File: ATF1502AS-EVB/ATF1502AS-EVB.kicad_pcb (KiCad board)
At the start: 2 copper layers, 25.4 x 50.8 mm, 17 parts, among them J1 Conn_02x03_Odd_Even, J2 Conn_01x20, J3 Conn_01x20, U1 ATF1502AS

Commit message: Update for upstream changes.
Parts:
- U1: value ATF1502AS -> ATF1502AS-xAx44

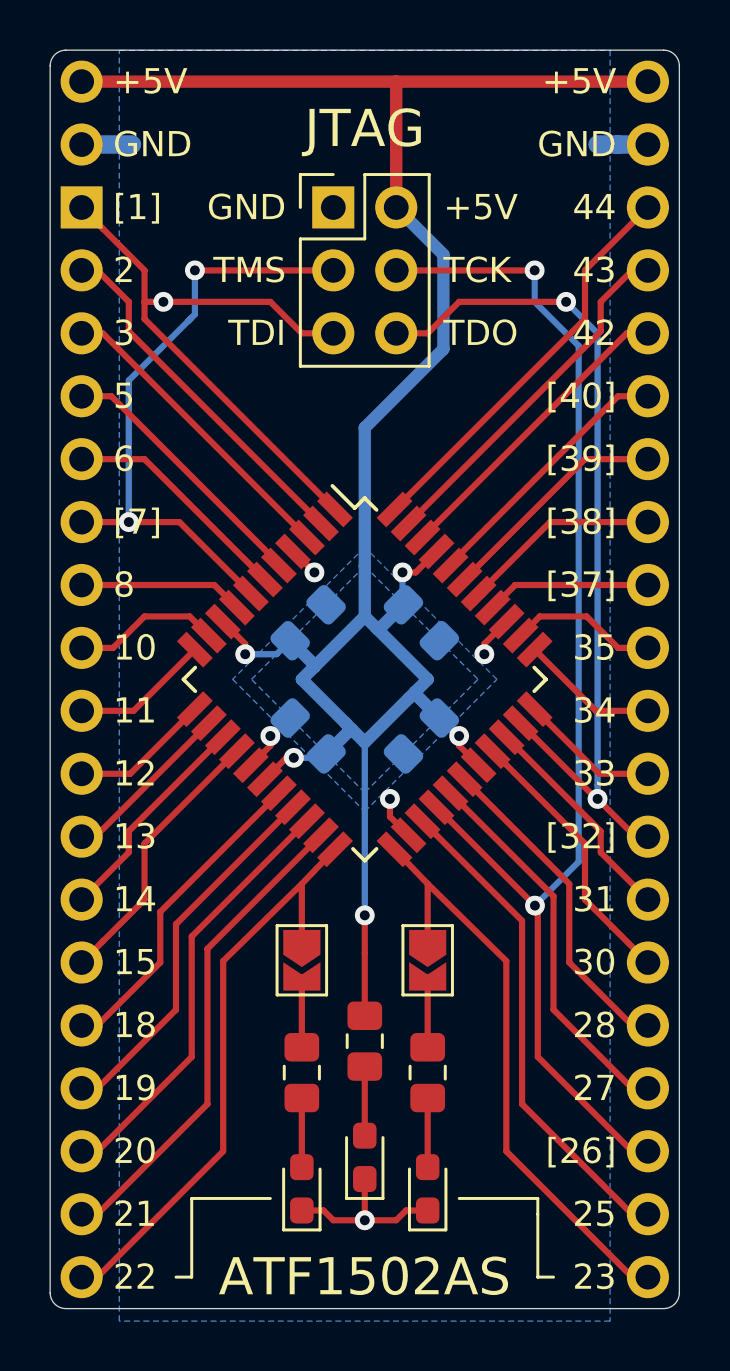
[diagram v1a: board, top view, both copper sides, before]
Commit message: ATF1502AS-EVB: final changes for fab.
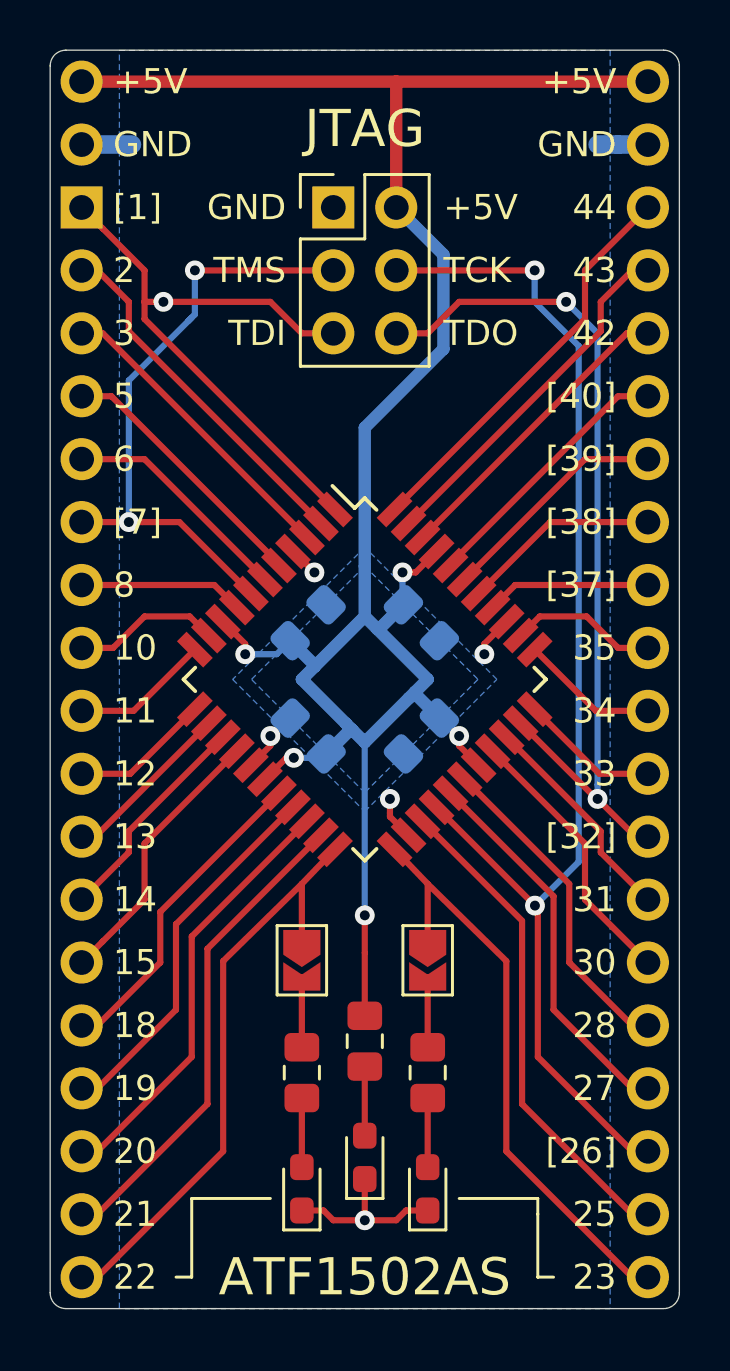
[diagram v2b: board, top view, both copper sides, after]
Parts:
- D1, D2, D3: value LED -> GRN
- J1: value Conn_02x03_Odd_Even -> VERT
- J2, J3: value Conn_01x20 -> VERT; footprint ATF1502AS-EVB:PinSocket_1x20_P2.54mm_Vertical_NoSilk -> ATF1502AS-EVB:PinHeader_1x20_P2.54mm_Vertical_NoSilk
- JP1, JP2: value SolderJumper_2_Open -> DNP
- R1, R2, R3: value 3k3 -> 10k
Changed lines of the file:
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@@
     (0 "F.Cu" signal)
     (31 "B.Cu" signal)
-    (32 "B.Adhes" user hide)
-    (33 "F.Adhes" user hide)
+    (32 "B.Adhes" user)
+    (33 "F.Adhes" user)
     (34 "B.Paste" user hide)
     (35 "F.Paste" user hide)
     (36 "B.SilkS" user)
     (37 "F.SilkS" user)
-    (38 "B.Mask" user hide)
-    (39 "F.Mask" user hide)
+    (38 "B.Mask" user)
+    (39 "F.Mask" user)
     (40 "Dwgs.User" user)
     (41 "Cmts.User" user hide)
@@
       (outputformat 1)
       (mirror false)
-      (drillshape 1)
+      (drillshape 0)
       (scaleselection 1)
-      (outputdirectory "")
+      (outputdirectory "Fab/")
     )
   )
@@
     (add_net "GND")
   )
-  (module "ATF1502AS-EVB:PinSocket_1x20_P2.54mm_Vertical_NoSilk" (layer "B.Cu")
+  (module "ATF1502AS-EVB:PinHeader_1x20_P2.54mm_Vertical_NoSilk" (layer "B.Cu")
     (at 73.66 50.8 180)
-    (descr "Through hole straight socket strip, 1x20, 2.54mm pitch, single row (from Kicad 4.0.7), script generated")
-    (tags "Through hole socket strip THT 1x20 2.54mm single row")
-    (fp_text reference "J3" (at 0 2.77) (layer "B.SilkS") hide
+    (descr "Through hole straight pin header, 1x20, 2.54mm pitch, single row")
+    (tags "Through hole pin header THT 1x20 2.54mm single row")
+    (fp_text reference "J3" (at 0 2.33) (layer "B.SilkS") hide
       (effects (font (size 1 1) (thickness 0.15)) (justify mirror))
     )
-    (fp_text value "Conn_01x20" (at 0 -51.03) (layer "B.Fab")
+    (fp_text value "VERT" (at 0 -50.59) (layer "B.Fab") hide
       (effects (font (size 1 1) (thickness 0.15)) (justify mirror))
     )
-    (fp_line (start -1.27 1.27) (end 0.635 1.27) (layer "B.Fab") (width 0.1))
-    (fp_line (start 0.635 1.27) (end 1.27 0.635) (layer "B.Fab") (width 0.1))
-    (fp_line (start 1.27 0.635) (end 1.27 -49.53) (layer "B.Fab") (width 0.1))
+    (fp_line (start -0.635 1.27) (end 1.27 1.27) (layer "B.Fab") (width 0.1))
+    (fp_line (start 1.27 1.27) (end 1.27 -49.53) (layer "B.Fab") (width 0.1))
     (fp_line (start 1.27 -49.53) (end -1.27 -49.53) (layer "B.Fab") (width 0.1))
-    (fp_line (start -1.27 -49.53) (end -1.27 1.27) (layer "B.Fab") (width 0.1))
-    (fp_line (start -1.8 1.8) (end 1.75 1.8) (layer "B.CrtYd") (width 0.05))
-    (fp_line (start 1.75 1.8) (end 1.75 -50) (layer "B.CrtYd") (width 0.05))
-    (fp_line (start 1.75 -50) (end -1.8 -50) (layer "B.CrtYd") (width 0.05))
-    (fp_line (start -1.8 -50) (end -1.8 1.8) (layer "B.CrtYd") (width 0.05))
+    (fp_line (start -1.27 -49.53) (end -1.27 0.635) (layer "B.Fab") (width 0.1))
+    (fp_line (start -1.27 0.635) (end -0.635 1.27) (layer "B.Fab") (width 0.1))
+    (fp_line (start -1.8 1.8) (end -1.8 -50.05) (layer "B.CrtYd") (width 0.05))
+    (fp_line (start -1.8 -50.05) (end 1.8 -50.05) (layer "B.CrtYd") (width 0.05))
+    (fp_line (start 1.8 -50.05) (end 1.8 1.8) (layer "B.CrtYd") (width 0.05))
+    (fp_line (start 1.8 1.8) (end -1.8 1.8) (layer "B.CrtYd") (width 0.05))
     (fp_text user "%R" (at 0 -24.13 270) (layer "B.Fab")
       (effects (font (size 1 1) (thickness 0.15)) (justify mirror))
@@
     (pad "1" thru_hole oval (at 0 0 180) (size 1.7 1.7) (drill 1) (layers *.Cu *.Mask)
       (net 2 "+5V"))
-    (model "${KISYS3DMOD}/Connector_PinSocket_2.54mm.3dshapes/PinSocket_1x20_P2.54mm_Vertical.wrl"
+    (model "${KISYS3DMOD}/Connector_PinHeader_2.54mm.3dshapes/PinHeader_1x20_P2.54mm_Vertical.wrl"
       (at (xyz 0 0 0))
       (scale (xyz 1 1 1))
@@
     )
   )
-  (module "ATF1502AS-EVB:PinSocket_1x20_P2.54mm_Vertical_NoSilk" (layer "B.Cu")
+  (module "ATF1502AS-EVB:PinHeader_1x20_P2.54mm_Vertical_NoSilk" (layer "B.Cu")
     (at 50.8 99.06)
-    (descr "Through hole straight socket strip, 1x20, 2.54mm pitch, single row (from Kicad 4.0.7), script generated")
-    (tags "Through hole socket strip THT 1x20 2.54mm single row")
-    (fp_text reference "J2" (at 0 2.77) (layer "B.SilkS") hide
+    (descr "Through hole straight pin header, 1x20, 2.54mm pitch, single row")
+    (tags "Through hole pin header THT 1x20 2.54mm single row")
+    (fp_text reference "J2" (at 0 2.33) (layer "B.SilkS") hide
       (effects (font (size 1 1) (thickness 0.15)) (justify mirror))
     )
-    (fp_text value "Conn_01x20" (at 0 -51.03) (layer "B.Fab")
+    (fp_text value "VERT" (at 0 -50.59) (layer "B.Fab") hide
       (effects (font (size 1 1) (thickness 0.15)) (justify mirror))
     )
-    (fp_line (start -1.27 1.27) (end 0.635 1.27) (layer "B.Fab") (width 0.1))
-    (fp_line (start 0.635 1.27) (end 1.27 0.635) (layer "B.Fab") (width 0.1))
-    (fp_line (start 1.27 0.635) (end 1.27 -49.53) (layer "B.Fab") (width 0.1))
+    (fp_line (start -0.635 1.27) (end 1.27 1.27) (layer "B.Fab") (width 0.1))
+    (fp_line (start 1.27 1.27) (end 1.27 -49.53) (layer "B.Fab") (width 0.1))
     (fp_line (start 1.27 -49.53) (end -1.27 -49.53) (layer "B.Fab") (width 0.1))
-    (fp_line (start -1.27 -49.53) (end -1.27 1.27) (layer "B.Fab") (width 0.1))
-    (fp_line (start -1.8 1.8) (end 1.75 1.8) (layer "B.CrtYd") (width 0.05))
-    (fp_line (start 1.75 1.8) (end 1.75 -50) (layer "B.CrtYd") (width 0.05))
-    (fp_line (start 1.75 -50) (end -1.8 -50) (layer "B.CrtYd") (width 0.05))
-    (fp_line (start -1.8 -50) (end -1.8 1.8) (layer "B.CrtYd") (width 0.05))
+    (fp_line (start -1.27 -49.53) (end -1.27 0.635) (layer "B.Fab") (width 0.1))
+    (fp_line (start -1.27 0.635) (end -0.635 1.27) (layer "B.Fab") (width 0.1))
+    (fp_line (start -1.8 1.8) (end -1.8 -50.05) (layer "B.CrtYd") (width 0.05))
+    (fp_line (start -1.8 -50.05) (end 1.8 -50.05) (layer "B.CrtYd") (width 0.05))
+    (fp_line (start 1.8 -50.05) (end 1.8 1.8) (layer "B.CrtYd") (width 0.05))
+    (fp_line (start 1.8 1.8) (end -1.8 1.8) (layer "B.CrtYd") (width 0.05))
     (fp_text user "%R" (at 0 -24.13 -90) (layer "B.Fab")
       (effects (font (size 1 1) (thickness 0.15)) (justify mirror))
@@
     (pad "1" thru_hole oval (at 0 0) (size 1.7 1.7) (drill 1) (layers *.Cu *.Mask)
       (net 38 "/LED1"))
-    (model "${KISYS3DMOD}/Connector_PinSocket_2.54mm.3dshapes/PinSocket_1x20_P2.54mm_Vertical.wrl"
+    (model "${KISYS3DMOD}/Connector_PinHeader_2.54mm.3dshapes/PinHeader_1x20_P2.54mm_Vertical.wrl"
       (at (xyz 0 0 0))
       (scale (xyz 1 1 1))
@@
       (effects (font (size 1 1) (thickness 0.15)))
     )
-    (fp_text value "SolderJumper_2_Open" (at 0 1.9 90) (layer "F.Fab")
+    (fp_text value "DNP" (at 0 1.9 90) (layer "F.Fab") hide
       (effects (font (size 1 1) (thickness 0.15)))
     )
@@
       (effects (font (size 1 1) (thickness 0.15)))
     )
-    (fp_text value "SolderJumper_2_Open" (at 0 1.9 90) (layer "F.Fab")
+    (fp_text value "DNP" (at 0 1.9 90) (layer "F.Fab") hide
       (effects (font (size 1 1) (thickness 0.15)))
     )
@@
       (effects (font (size 1 1) (thickness 0.15)))
     )
-    (fp_text value "3k3" (at 0 1.65 90) (layer "F.Fab")
+    (fp_text value "10k" (at 0 -1.778 90) (layer "F.Fab")
       (effects (font (size 1 1) (thickness 0.15)))
     )
@@
       (effects (font (size 1 1) (thickness 0.15)))
     )
-    (fp_text value "3k3" (at 0 1.65 90) (layer "F.Fab")
+    (fp_text value "10k" (at -3.429 0 90) (layer "F.Fab")
       (effects (font (size 1 1) (thickness 0.15)))
     )
@@
       (effects (font (size 1 1) (thickness 0.15)))
     )
-    (fp_text value "3k3" (at 0 1.65 90) (layer "F.Fab")
+    (fp_text value "10k" (at 0 1.65 90) (layer "F.Fab")
       (effects (font (size 1 1) (thickness 0.15)))
     )
@@
       (effects (font (size 1 1) (thickness 0.15)))
     )
-    (fp_text value "LED" (at 0 1.43 90) (layer "F.Fab")
+    (fp_text value "GRN" (at 0 1.43 90) (layer "F.Fab")
       (effects (font (size 1 1) (thickness 0.15)))
     )
@@
       (effects (font (size 1 1) (thickness 0.15)))
     )
-    (fp_text value "LED" (at 0 1.43 90) (layer "F.Fab")
+    (fp_text value "GRN" (at -3.311 0 90) (layer "F.Fab")
       (effects (font (size 1 1) (thickness 0.15)))
     )
@@
       (effects (font (size 1 1) (thickness 0.15)))
     )
-    (fp_text value "LED" (at 0 1.43 90) (layer "F.Fab")
+    (fp_text value "GRN" (at 0 -1.524 90) (layer "F.Fab")
       (effects (font (size 1 1) (thickness 0.15)))
     )
@@
       (effects (font (size 1 1) (thickness 0.15)))
     )
-    (fp_text value "ATF1502AS-xAx44" (at 0 7.450001 135) (layer "F.Fab")
+    (fp_text value "ATF1502AS-xAx44" (at -1.436841 -7.543415 135) (layer "F.Fab")
       (effects (font (size 1 1) (thickness 0.15)))
     )
@@
       (effects (font (size 1 1) (thickness 0.15)))
     )
-    (fp_text value "Conn_02x03_Odd_Even" (at 1.27 7.41) (layer "F.Fab") hide
+    (fp_text value "VERT" (at 1.27 7.41) (layer "F.Fab") hide
       (effects (font (size 1 1) (thickness 0.15)))
     )
@@
     (polygon
       (pts
-        (xy 72.136 100.838) (xy 52.324 100.838) (xy 52.324 49.53) (xy 72.136 49.53)
+        (xy 72.136 100.33) (xy 52.324 100.33) (xy 52.324 49.53) (xy 72.136 49.53)
       )
     )

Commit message: Modify silkscreen for 3v3 and 5v parts.
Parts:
- moved REF** 3.70 mm to (62.2, 83.9)
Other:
- net class Default removed
- net class Power removed
- board text added: "+3V3 +5V"
- board text added: "ASV(L) AS"
- board text added: "ATF15xxAS(V)"
- board text added: "VCC"
- board text removed: "+5V"
- board text removed: "ATF1502AS"
